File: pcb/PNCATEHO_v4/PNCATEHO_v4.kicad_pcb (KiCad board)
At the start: 2 copper layers, 93.5 x 54.1 mm, 27 parts, among them J1 TestPoint_2Pole, SW1 SW_PUSH, SW10 SW_PUSH, SW2 SW_PUSH, SW3 SW_PUSH, SW4 SW_PUSH, SW5 SW_PUSH, SW6 SW_PUSH, SW7 SW_PUSH, SW8 SW_PUSH, SW9 SW_PUSH, U1 ProMicro_r

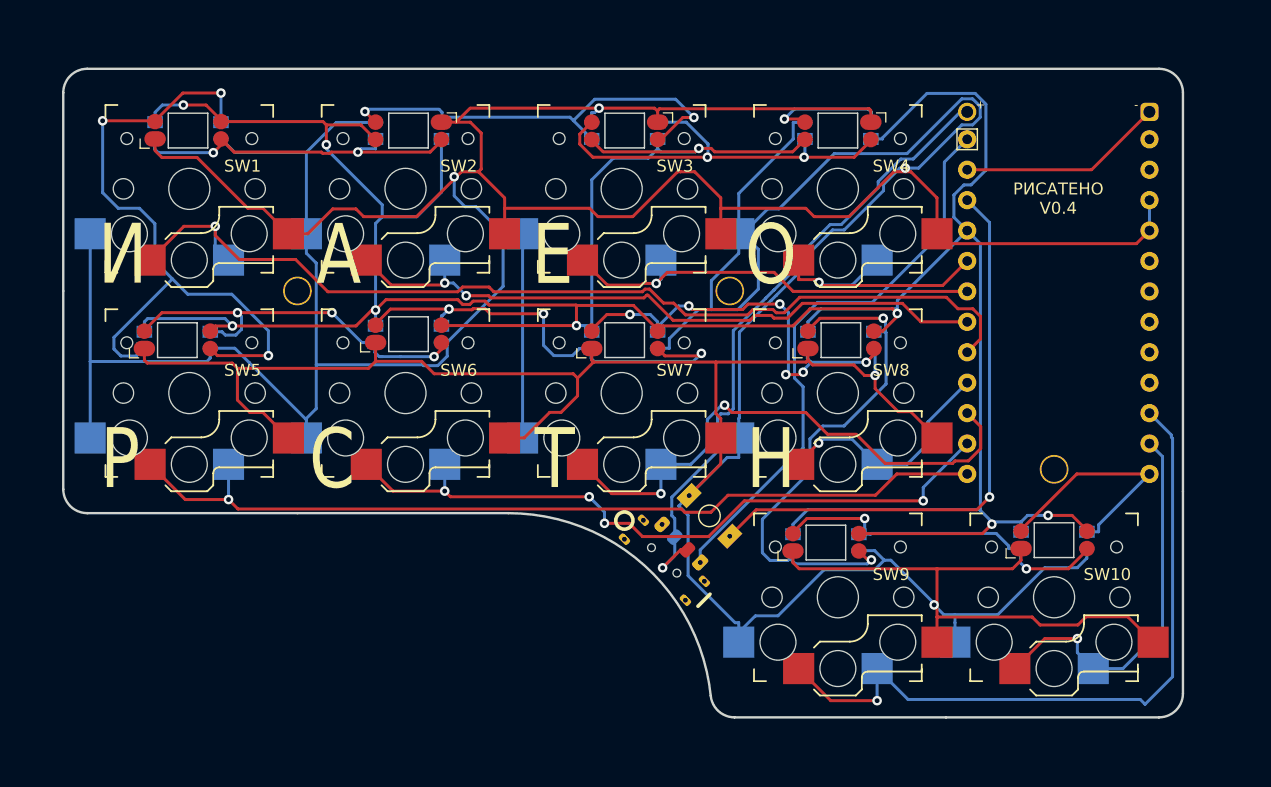
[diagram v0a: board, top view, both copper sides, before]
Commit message: Library change, change to hs switches, led changes
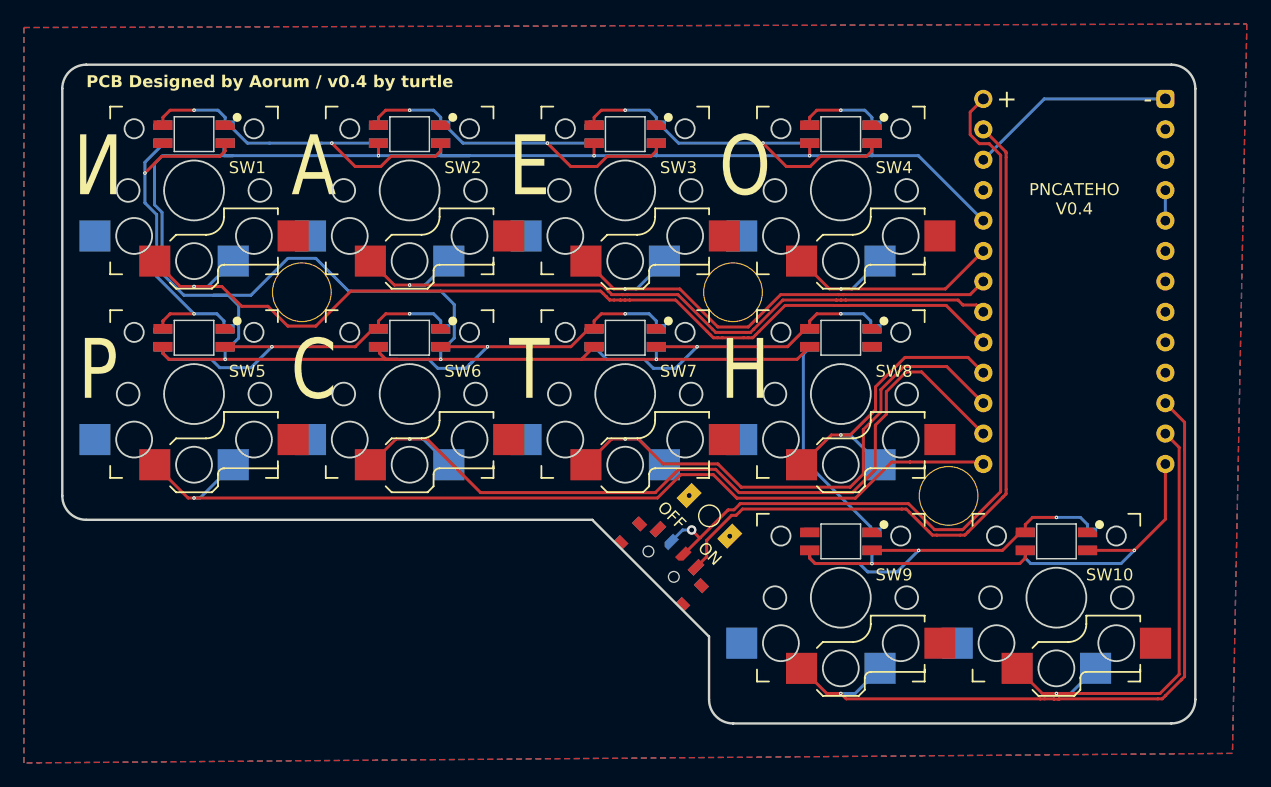
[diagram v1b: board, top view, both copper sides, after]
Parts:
- H1, H2, H3: footprint enki_lib:HOLE -> PNCATEHO:Hole
- J1: footprint enki_lib:battery_conn -> PNCATEHO:battery_conn_duplex
- PSW1: footprint enki_lib:switch_MSK-12C02_smd -> PNCATEHO:MSK-12C02_DUAL
- SW1, SW10, SW2, SW3, SW4, SW5, SW6, SW7, SW8, SW9: footprint keyswitches-pretty:Kailh_socket_PG1350_reversible -> PNCATEHO:Kailh_socket_PG1350_reversible
- moved J1 14.2 mm to (113.5, 43.6), turned to 0 degrees
- moved H3 9.09 mm to (103.0, 61.5)
- moved U1 2.93 mm to (113.5, 43.6)
- moved PSW1 1.67 mm to (78.1, 68.1), turned to 135 degrees
- moved LED6 1.41 mm to (40.0, 48.3), turned to 0 degrees
- moved LED2 1.25 mm to (94.0, 65.3), turned to 0 degrees
- moved LED7 0.58 mm to (40.0, 31.3), turned to 0 degrees
- moved SW1 0.42 mm to (40.0, 36.0)
- moved SW5 0.40 mm to (40.0, 53.0)
- moved LED10 0.39 mm to (94.0, 31.3)
- moved H1 0.38 mm to (49.0, 44.5)
- moved SW2 0.37 mm to (58.0, 36.0)
- moved SW6 0.35 mm to (58.0, 53.0)
- moved SW3 0.32 mm to (76.0, 36.0)
- moved LED8 0.31 mm to (58.0, 31.3)
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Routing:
- net GND: track 597.6 -> 2.54 mm, vias 5 -> 0
- net VCC: track 284.4 -> 216.2 mm, vias 9 -> 7
- net reset: track 48.6 -> 0.00 mm, vias 1 -> 0
- net Net-(LED2-DOUT): track 44.7 -> 18.1 mm, vias 2 -> 0
- net Net-(LED6-DOUT): track 57.8 -> 31.6 mm, vias 3 -> 2
- net Net-(PSW1-B): track 53.4 -> 68.4 mm
- net VBAT: track 47.9 -> 62.3 mm
- net R2C2: track 59.3 -> 69.3 mm, vias 4 -> 1
- net R3C5: track 32.4 -> 39.8 mm
- net Net-(LED4-DOUT): track 38.2 -> 32.5 mm, vias 3 -> 2
- net R2C4: track 19.8 -> 24.8 mm
- net R1C3: track 36.2 -> 41.3 mm
- net Net-(LED8-DOUT): track 37.2 -> 32.1 mm
- net Net-(LED3-DOUT): track 34.7 -> 30.9 mm, vias 6 -> 2
- net R2C1: track 74.1 -> 77.7 mm
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- added copper zone on B.Cu, net GND
- added copper zone on F.Cu, net GND
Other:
- board size 93.5 x 54.1 mm -> 94.6 x 55 mm
- board text added: "PCB Designed by Aorum / v0.4 by turtle"
- board text added: "PNCATEHO V0.4"
- board text removed: "PCB designed by Aroum"
- board text removed: "X-key"
- board text removed: "РИСАТЕНО V0.4"

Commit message: Almosta all routed
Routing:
- net reset: track 0.00 -> 60.9 mm
- net GND: track 2.54 -> 33.4 mm, vias 0 -> 6
- net VCC: track 216.2 -> 245.7 mm, vias 7 -> 8
- net Net-(LED2-DOUT): track 18.1 -> 32.4 mm, vias 0 -> 2
